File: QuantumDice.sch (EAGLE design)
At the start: 35 parts, among them IC2 LM1117IMPX-3.3, IC3 LM358MX, IC5 MC34063AP

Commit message: PCB updated
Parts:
- removed D1: (no value), diode:DIODE-SMB
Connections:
- net A_3V renamed A_5V
- net _3V renamed _5V
- removed net VBUS: C11.+, C30.1, C7.+, C8.1, D1.C, F3.2, IC2.IN, IC5.VCC, R25.1
- new net 9V: C11.+, C30.1, C7.+, C8.1, F3.2, IC2.IN, IC5.VCC, R25.1
- net GND: no longer D1.A
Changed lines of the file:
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@@
 <part name="C34" library="rcl" deviceset="C-EU" device="050-024X044"/>
 <part name="JP4" library="SparkFun-Connectors" deviceset="USB_MICROB_PLUG" device="CONN-11752"/>
-<part name="D1" library="diode" deviceset="DIODE-" device="SMB"/>
-<part name="GND53" library="supply1" deviceset="GND" device=""/>
 <part name="U$5" library="mw" deviceset="STS5" device=""/>
 </parts>
@@
 <instance part="C34" gate="G$1" x="218.44" y="-304.8"/>
 <instance part="JP4" gate="G$1" x="68.58" y="-220.98" rot="MR0"/>
-<instance part="D1" gate="G$1" x="93.98" y="-223.52" rot="R90"/>
-<instance part="GND53" gate="1" x="93.98" y="-233.68"/>
 <instance part="U$5" gate="G$1" x="276.86" y="-299.72"/>
 </instances>
@@
 <pinref part="U$5" gate="G$1" pin="-"/>
 </segment>
-<segment>
-<pinref part="D1" gate="G$1" pin="A"/>
-<pinref part="GND53" gate="1" pin="GND"/>
-<wire x1="93.98" y1="-231.14" x2="93.98" y2="-226.06" width="0.1524" layer="91"/>
-</segment>
 </net>
 <net name="N$14" class="0">
@@
 </segment>
 </net>
-<net name="_3V" class="0">
+<net name="_5V" class="0">
 <segment>
 <pinref part="C9" gate="G$1" pin="1"/>
@@
 </segment>
 </net>
-<net name="VBUS" class="0">
+<net name="9V" class="0">
 <segment>
 <pinref part="F3" gate="G$1" pin="2"/>
-<wire x1="91.44" y1="-215.9" x2="93.98" y2="-215.9" width="0.1524" layer="91"/>
-<wire x1="93.98" y1="-215.9" x2="101.6" y2="-215.9" width="0.1524" layer="91"/>
+<wire x1="91.44" y1="-215.9" x2="101.6" y2="-215.9" width="0.1524" layer="91"/>
 <wire x1="124.46" y1="-215.9" x2="116.84" y2="-215.9" width="0.1524" layer="91"/>
 <pinref part="C7" gate="G$1" pin="+"/>
@@
 <junction x="116.84" y="-215.9"/>
 <pinref part="IC2" gate="G$1" pin="IN"/>
-<pinref part="D1" gate="G$1" pin="C"/>
-<wire x1="93.98" y1="-220.98" x2="93.98" y2="-215.9" width="0.1524" layer="91"/>
-<junction x="93.98" y="-215.9"/>
 </segment>
 <segment>
@@
 </segment>
 </net>
-<net name="A_3V" class="0">
+<net name="A_5V" class="0">
 <segment>
 <pinref part="R18" gate="G$1" pin="2"/>

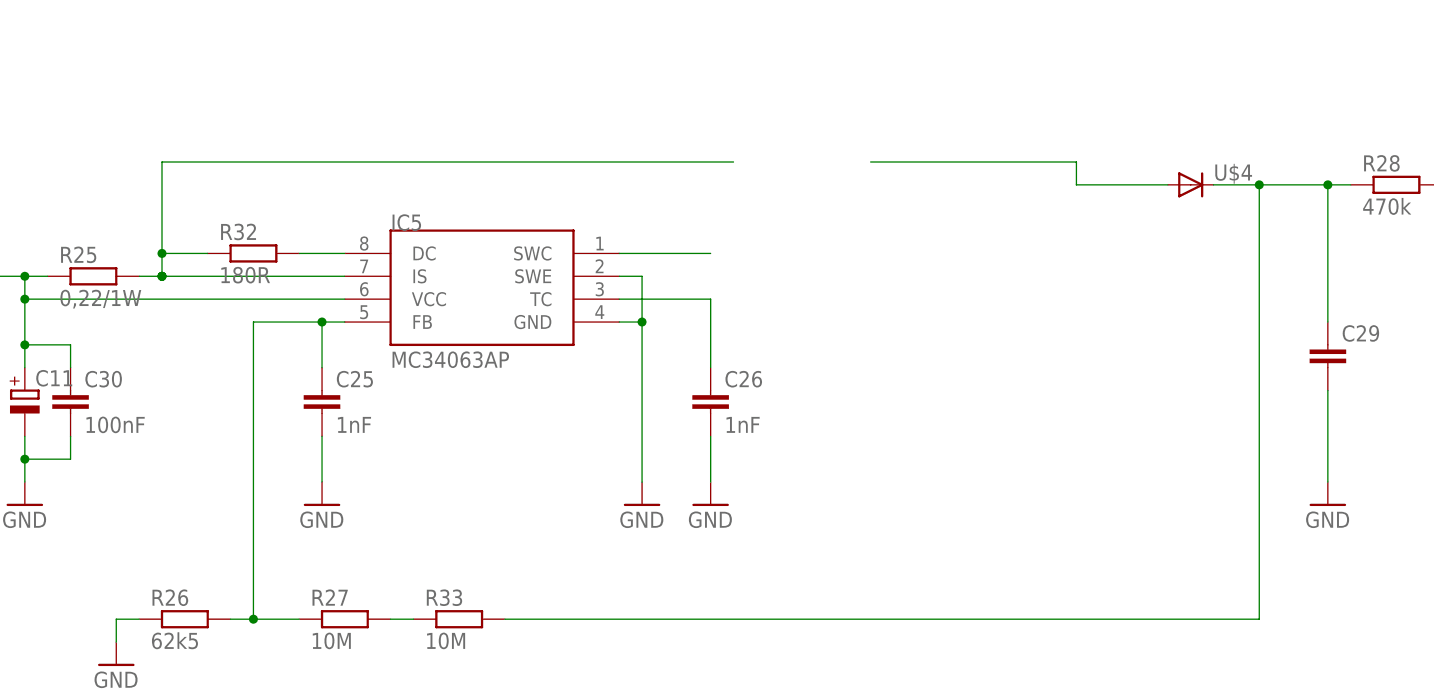
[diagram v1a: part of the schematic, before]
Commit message: Power circuit updated
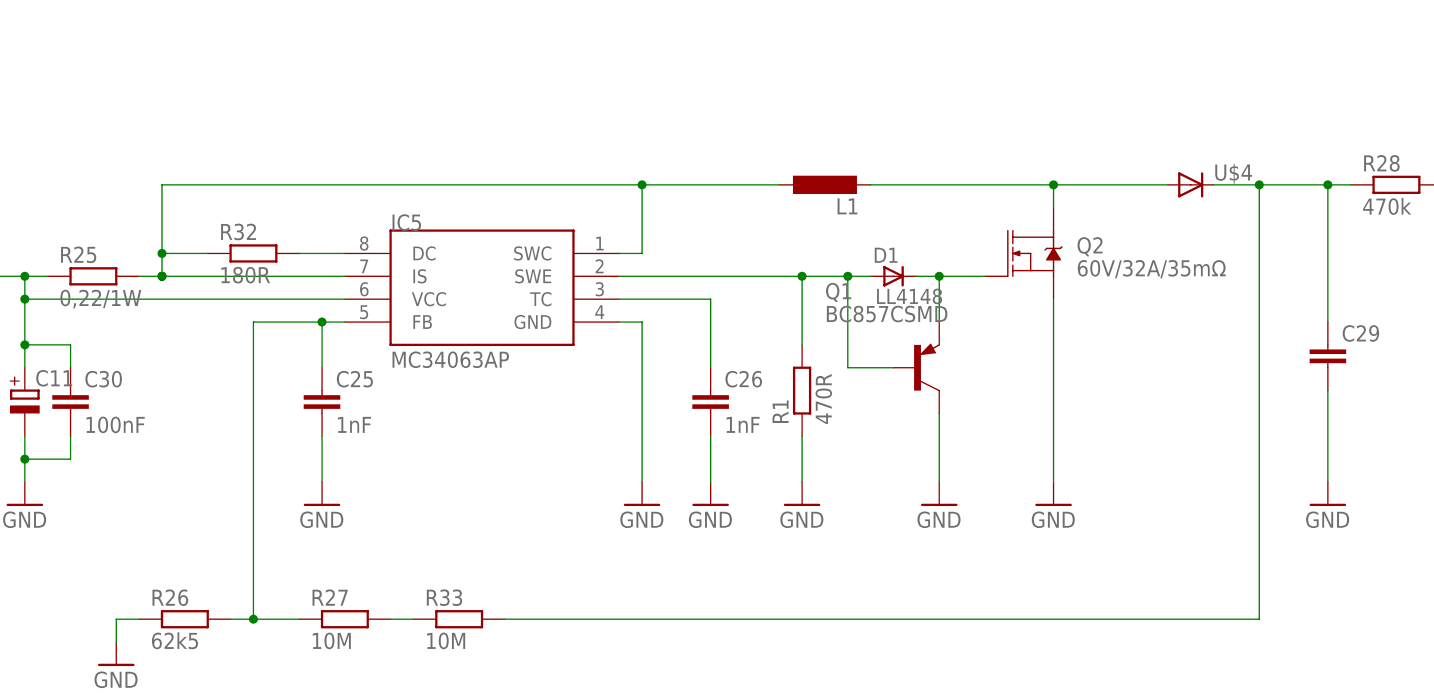
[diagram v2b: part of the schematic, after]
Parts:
- added D1: LL4148, _hhn_diodes_smd:LL4148
- added L1: (no value), rcl:L-EU6000-XXX-RC
- added Q1: BC857CSMD, transistor-pnp:BC857CSMD
- added Q2: 60V/32A/35mΩ, SparkFun-DiscreteSemi:MOSFET-NCH-FQP30N06L
- added R1: 470R, rcl:R-EU_R1206
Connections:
- removed net N$4: IC5.IS, R25.2, R32.1
- new net N$2: D1.A, IC5.SWE, Q1.B, R1.2
- new net N$3: D1.C, Q1.E, Q2.G
- net GND: now also Q1.C, Q2.S, R1.1; no longer IC5.SWE
- net N$21: now also L1.2, Q2.D
- net N$33: now also IC5.IS, L1.1, R25.2, R32.1
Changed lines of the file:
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@@
 <layer number="154" name="FabDoc2" color="7" fill="1" visible="yes" active="yes"/>
 <layer number="155" name="FabDoc3" color="7" fill="1" visible="yes" active="yes"/>
+<layer number="156" name="gesam-Maß" color="1" fill="7" visible="no" active="no"/>
+<layer number="157" name="FaceMchng" color="3" fill="1" visible="no" active="no"/>
+<layer number="158" name="FaceMMeas" color="3" fill="1" visible="no" active="no"/>
+<layer number="159" name="Geh-Bear2" color="1" fill="7" visible="no" active="no"/>
+<layer number="160" name="Topologie" color="9" fill="1" visible="no" active="no"/>
+<layer number="161" name="tomplace2" color="7" fill="1" visible="no" active="no"/>
 <layer number="191" name="mNets" color="7" fill="1" visible="yes" active="yes"/>
 <layer number="192" name="mBusses" color="7" fill="1" visible="yes" active="yes"/>
@@
 <layer number="250" name="Descript" color="3" fill="1" visible="no" active="no"/>
 <layer number="251" name="SMDround" color="12" fill="11" visible="no" active="no"/>
+<layer number="252" name="BR-BS" color="7" fill="1" visible="no" active="no"/>
+<layer number="253" name="BR-LS" color="7" fill="1" visible="no" active="no"/>
 <layer number="254" name="cooling" color="7" fill="1" visible="yes" active="yes"/>
 <layer number="255" name="HELP" color="7" fill="1" visible="yes" active="yes"/>
@@
 <part name="JP4" library="SparkFun-Connectors" deviceset="USB_MICROB_PLUG" device="CONN-11752"/>
 <part name="U$5" library="mw" deviceset="STS5" device=""/>
+<part name="L1" library="rcl" deviceset="L-EU" device="6000-XXX-RC"/>
+<part name="GND1" library="supply1" deviceset="GND" device=""/>
+<part name="R1" library="rcl" deviceset="R-EU_" device="R1206" value="470R"/>
+<part name="D1" library="_hhn_diodes_smd" deviceset="LL4148" device=""/>
+<part name="Q1" library="transistor-pnp" deviceset="BC857*" device="SMD" technology="C"/>
+<part name="GND2" library="supply1" deviceset="GND" device=""/>
+<part name="Q2" library="SparkFun-DiscreteSemi" deviceset="MOSFET-NCH" device="-FQP30N06L" value="60V/32A/35mΩ"/>
+<part name="GND3" library="supply1" deviceset="GND" device=""/>
 </parts>
 <sheets>
@@
 <instance part="JP4" gate="G$1" x="68.58" y="-220.98" rot="MR0"/>
 <instance part="U$5" gate="G$1" x="276.86" y="-299.72"/>
+<instance part="L1" gate="G$1" x="147.32" y="-299.72" rot="R90"/>
+<instance part="GND1" gate="1" x="144.78" y="-335.28"/>
+<instance part="R1" gate="G$1" x="144.78" y="-322.58" rot="R90"/>
+<instance part="D1" gate="G$1" x="154.94" y="-309.88"/>
+<instance part="Q1" gate="G$1" x="157.48" y="-320.04"/>
+<instance part="GND2" gate="1" x="160.02" y="-335.28"/>
+<instance part="Q2" gate="NMOS" x="170.18" y="-307.34"/>
+<instance part="GND3" gate="1" x="172.72" y="-335.28"/>
 </instances>
 <busses>
@@
 <wire x1="124.46" y1="-314.96" x2="127" y2="-314.96" width="0.1524" layer="91"/>
 <wire x1="127" y1="-314.96" x2="127" y2="-332.74" width="0.1524" layer="91"/>
-<pinref part="IC5" gate="G$1" pin="SWE"/>
-<wire x1="124.46" y1="-309.88" x2="127" y2="-309.88" width="0.1524" layer="91"/>
-<wire x1="127" y1="-309.88" x2="127" y2="-314.96" width="0.1524" layer="91"/>
-<junction x="127" y="-314.96"/>
 </segment>
 <segment>
@@
 <wire x1="304.8" y1="-299.72" x2="294.64" y2="-299.72" width="0.1524" layer="91"/>
 <pinref part="U$5" gate="G$1" pin="-"/>
+</segment>
+<segment>
+<pinref part="GND1" gate="1" pin="GND"/>
+<wire x1="144.78" y1="-332.74" x2="144.78" y2="-327.66" width="0.1524" layer="91"/>
+<pinref part="R1" gate="G$1" pin="1"/>
+</segment>
+<segment>
+<pinref part="Q1" gate="G$1" pin="C"/>
+<pinref part="GND2" gate="1" pin="GND"/>
+<wire x1="160.02" y1="-332.74" x2="160.02" y2="-325.12" width="0.1524" layer="91"/>
+</segment>
+<segment>
+<pinref part="Q2" gate="NMOS" pin="S"/>
+<pinref part="GND3" gate="1" pin="GND"/>
+<wire x1="172.72" y1="-332.74" x2="172.72" y2="-312.42" width="0.1524" layer="91"/>
 </segment>
 </net>
@@
 </segment>
 </net>
-<net name="N$4" class="0">
-<segment>
-<pinref part="IC5" gate="G$1" pin="IS"/>
-<pinref part="R25" gate="G$1" pin="2"/>
-<wire x1="93.98" y1="-309.88" x2="73.66" y2="-309.88" width="0.1524" layer="91"/>
-<wire x1="73.66" y1="-309.88" x2="71.12" y2="-309.88" width="0.1524" layer="91"/>
-<junction x="73.66" y="-309.88"/>
-<wire x1="73.66" y1="-309.88" x2="73.66" y2="-307.34" width="0.1524" layer="91"/>
-<wire x1="73.66" y1="-307.34" x2="73.66" y2="-297.18" width="0.1524" layer="91"/>
-<junction x="73.66" y="-309.88"/>
-<wire x1="137.16" y1="-297.18" x2="73.66" y2="-297.18" width="0.1524" layer="91"/>
-<pinref part="R32" gate="G$1" pin="1"/>
-<wire x1="78.74" y1="-307.34" x2="73.66" y2="-307.34" width="0.1524" layer="91"/>
-<junction x="73.66" y="-307.34"/>
-</segment>
-</net>
 <net name="N$11" class="0">
 <segment>
@@
 <net name="N$21" class="0">
 <segment>
-<wire x1="152.4" y1="-297.18" x2="175.26" y2="-297.18" width="0.1524" layer="91"/>
-<wire x1="175.26" y1="-297.18" x2="175.26" y2="-299.72" width="0.1524" layer="91"/>
-<wire x1="175.26" y1="-299.72" x2="185.42" y2="-299.72" width="0.1524" layer="91"/>
+<wire x1="152.4" y1="-299.72" x2="172.72" y2="-299.72" width="0.1524" layer="91"/>
 <pinref part="U$4" gate="G$1" pin="A"/>
+<pinref part="L1" gate="G$1" pin="2"/>
+<pinref part="Q2" gate="NMOS" pin="D"/>
+<wire x1="172.72" y1="-299.72" x2="185.42" y2="-299.72" width="0.1524" layer="91"/>
+<wire x1="172.72" y1="-302.26" x2="172.72" y2="-299.72" width="0.1524" layer="91"/>
+<junction x="172.72" y="-299.72"/>
 </segment>
 </net>
@@
 <segment>
 <pinref part="IC5" gate="G$1" pin="SWC"/>
-<wire x1="134.62" y1="-307.34" x2="124.46" y2="-307.34" width="0.1524" layer="91"/>
+<wire x1="127" y1="-307.34" x2="124.46" y2="-307.34" width="0.1524" layer="91"/>
+<pinref part="IC5" gate="G$1" pin="IS"/>
+<pinref part="R25" gate="G$1" pin="2"/>
+<wire x1="93.98" y1="-309.88" x2="73.66" y2="-309.88" width="0.1524" layer="91"/>
+<wire x1="73.66" y1="-309.88" x2="71.12" y2="-309.88" width="0.1524" layer="91"/>
+<junction x="73.66" y="-309.88"/>
+<wire x1="73.66" y1="-309.88" x2="73.66" y2="-307.34" width="0.1524" layer="91"/>
+<wire x1="73.66" y1="-307.34" x2="73.66" y2="-299.72" width="0.1524" layer="91"/>
+<junction x="73.66" y="-309.88"/>
+<wire x1="142.24" y1="-299.72" x2="127" y2="-299.72" width="0.1524" layer="91"/>
+<pinref part="R32" gate="G$1" pin="1"/>
+<wire x1="127" y1="-299.72" x2="73.66" y2="-299.72" width="0.1524" layer="91"/>
+<wire x1="78.74" y1="-307.34" x2="73.66" y2="-307.34" width="0.1524" layer="91"/>
+<junction x="73.66" y="-307.34"/>
+<wire x1="127" y1="-307.34" x2="127" y2="-299.72" width="0.1524" layer="91"/>
+<junction x="127" y="-299.72"/>
+<pinref part="L1" gate="G$1" pin="1"/>
 </segment>
 </net>
@@
 </segment>
 </net>
+<net name="N$2" class="0">
+<segment>
+<pinref part="IC5" gate="G$1" pin="SWE"/>
+<wire x1="124.46" y1="-309.88" x2="144.78" y2="-309.88" width="0.1524" layer="91"/>
+<wire x1="144.78" y1="-309.88" x2="149.86" y2="-309.88" width="0.1524" layer="91"/>
+<wire x1="149.86" y1="-309.88" x2="152.4" y2="-309.88" width="0.1524" layer="91"/>
+<wire x1="144.78" y1="-317.5" x2="144.78" y2="-309.88" width="0.1524" layer="91"/>
+<junction x="144.78" y="-309.88"/>
+<pinref part="R1" gate="G$1" pin="2"/>
+<pinref part="D1" gate="G$1" pin="A"/>
+<pinref part="Q1" gate="G$1" pin="B"/>
+<wire x1="154.94" y1="-320.04" x2="149.86" y2="-320.04" width="0.1524" layer="91"/>
+<wire x1="149.86" y1="-320.04" x2="149.86" y2="-309.88" width="0.1524" layer="91"/>
+<junction x="149.86" y="-309.88"/>
+</segment>
+</net>
+<net name="N$3" class="0">
+<segment>
+<pinref part="D1" gate="G$1" pin="C"/>
+<pinref part="Q1" gate="G$1" pin="E"/>
+<wire x1="157.48" y1="-309.88" x2="160.02" y2="-309.88" width="0.1524" layer="91"/>
+<wire x1="160.02" y1="-309.88" x2="160.02" y2="-314.96" width="0.1524" layer="91"/>
+<pinref part="Q2" gate="NMOS" pin="G"/>
+<wire x1="165.1" y1="-309.88" x2="160.02" y2="-309.88" width="0.1524" layer="91"/>
+<junction x="160.02" y="-309.88"/>
+</segment>
+</net>

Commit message: Small updates
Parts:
- removed JP4: USB_MICROB_PLUGCONN-11752, SparkFun-Connectors:USB_MICROB_PLUGCONN-11752
- added C1, C2, C3, C4: (no value), rcl:C-EUC0603
- added IC4: MEGA8-AI, atmel:MEGA8-AI
- added J1: AVR_SPI_PRG_6PTH, SparkFun-Connectors:AVR_SPI_PRG_6PTH
- added R2: (no value), rcl:R-EU_R0603
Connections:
- new net MISO: IC4.PB4(MISO), J1.1
- new net MOSI: IC4.PB3(MOSI/OC2), J1.4
- new net N$6: C4.1, IC4.AREF
- new net RESET: IC4.PC6(/RESET), J1.5, R2.1
- new net SCK: IC4.PB5(SCK), J1.3
- net CPM: now also IC4.PD2(INT0)
- net GND: now also C1.2, C2.2, C3.2, C4.2, IC4.GND, IC4.GND@1, IC4.GND@2, J1.6; no longer JP4.GND
- net N$14: no longer JP4.VCC
- net _5V: now also C1.1, C2.1, C3.1, IC4.AVCC, IC4.VCC@1, IC4.VCC@2, J1.2, R2.2
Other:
- moved on the sheet: C10, C7, C8, C9
